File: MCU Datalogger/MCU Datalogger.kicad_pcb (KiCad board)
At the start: 2 copper layers, 50.8 x 30.5 mm, 30 parts, among them J1 Conn_01x04_Pin, J2 Conn_01x09_Pin, J3 Conn_01x04_Pin, J4 Conn_02x03_Odd_Even, U1 24LC1025, U2 DS1337S_, U3 24LC1025, U4 ATMEGA328P-AU, Y1 32.768KHz, Y2 16MHz

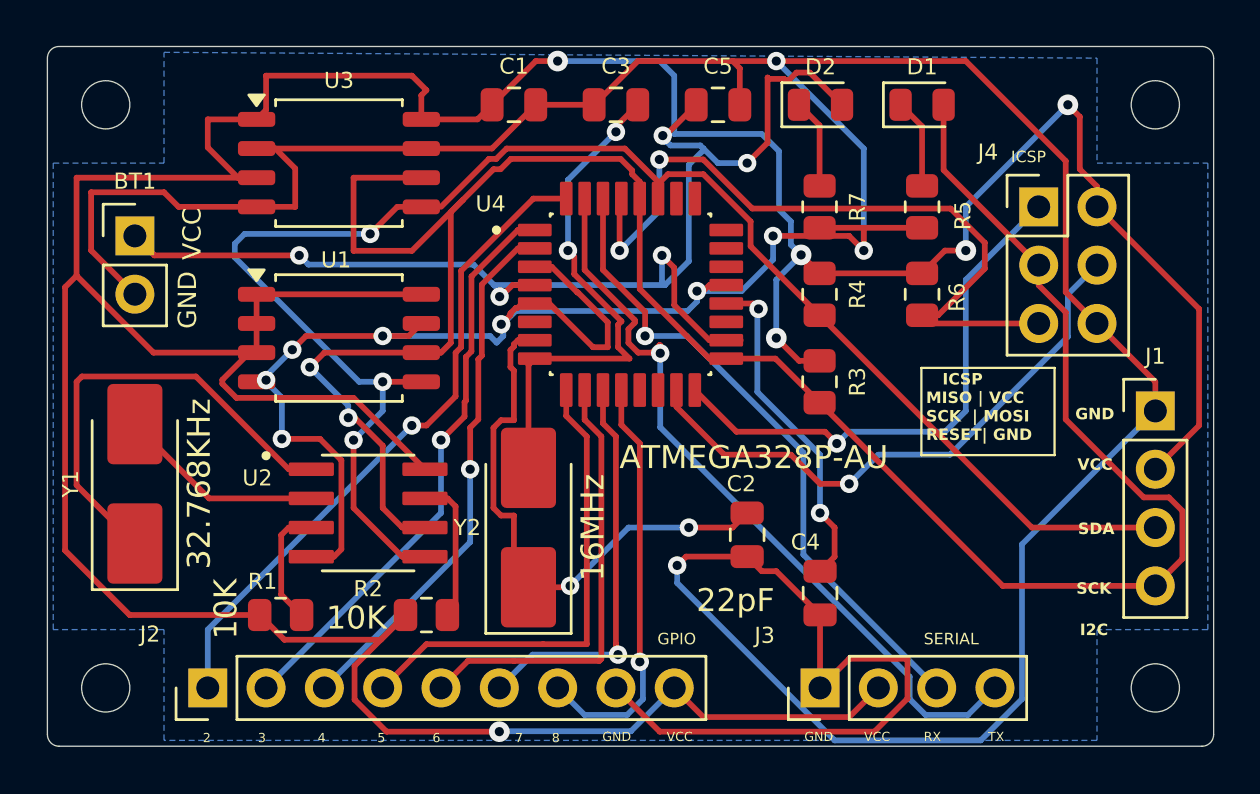
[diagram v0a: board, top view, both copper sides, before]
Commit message: 4layer: Completed 4layer routing of MCUdatalogger
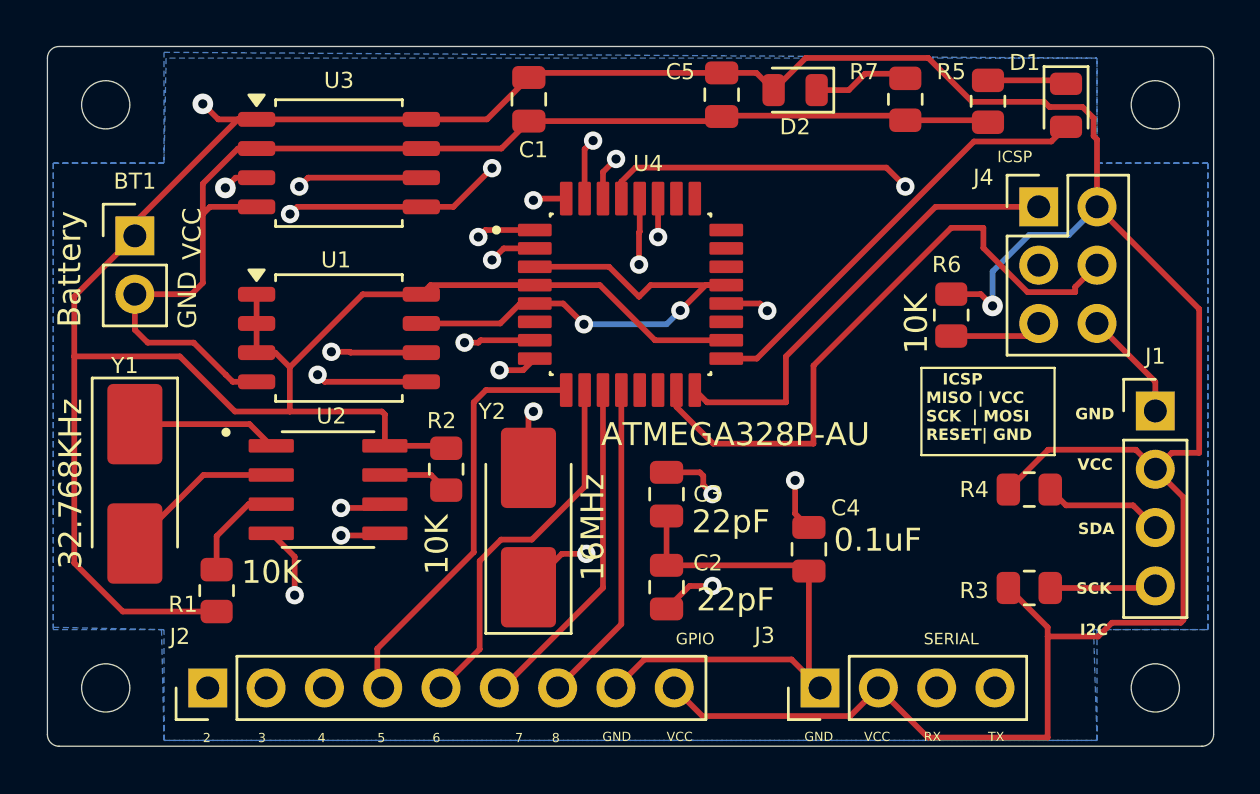
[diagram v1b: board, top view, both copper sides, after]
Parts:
- moved C3 17.1 mm to (140.0, 108.4), turned to 90 degrees
- moved R3 12.8 mm to (155.8, 112.5), turned to 0 degrees
- moved R4 12.5 mm to (155.8, 108.2), turned to 0 degrees
- moved R2 6.41 mm to (130.4, 107.3), turned to -90 degrees
- moved D1 6.27 mm to (157.4, 91.5), turned to -90 degrees
- moved R7 5.99 mm to (150.4, 91.2)
- moved R5 5.42 mm to (154.0, 91.3)
- moved C2 4.19 mm to (140.0, 112.5), turned to -90 degrees
- moved R1 2.99 mm to (120.4, 112.6), turned to 90 degrees
- moved U2 2.02 mm to (125.3, 108.2)
- moved C4 1.97 mm to (146.2, 110.8)
- moved R6 1.56 mm to (152.4, 100.6)
- moved D2 1.28 mm to (145.6, 90.8), turned to 180 degrees
- moved C1 0.69 mm to (134.0, 91.2), turned to -90 degrees
- moved C5 0.47 mm to (142.4, 91.0), turned to -90 degrees
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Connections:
- D1 pad 2: /SCK -> /D9
- U4 pad 17: /SCK -> /D9
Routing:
- net GND: track 208.0 -> 108.8 mm, vias 10 -> 3
- net /Vcc: track 240.0 -> 199.1 mm, vias 11 -> 3
- net /D9: track 0.00 -> 19.0 mm
- net Net-(U2-X1): track 20.1 -> 6.33 mm
- net /RX: track 28.4 -> 37.0 mm
- net /TX: track 34.0 -> 40.7 mm
- net /RESET: track 32.6 -> 26.1 mm, vias 2 -> 1
- net /SCK: track 102.5 -> 96.5 mm, vias 2 -> 4
- net /D8: track 18.3 -> 14.1 mm, vias 1 -> 0
- net Net-(U4-PB7): track 22.5 -> 18.6 mm, vias 2 -> 3
- net /MISO: track 23.6 -> 19.9 mm, vias 1 -> 0
- net Net-(U2-SQW/~INT): track 6.36 -> 2.94 mm
- net /D6: track 19.5 -> 16.4 mm
- net /D7: track 17.6 -> 14.9 mm, vias 1 -> 0
- net /D5: track 21.1 -> 18.5 mm
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- added copper zone on B.Cu, net GND
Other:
- copper layers 2 -> 4
- board text removed: "0.2000 mm / 0.0000 mm"
- board text removed: "0.3000 mm"
- board text removed: "1.6000 mm"
- board text removed: "50.8000 mm x 30.4800 mm"
- board text removed: "BOARD CHARACTERISTICS"
- board text removed: "Board Thickness:"
- board text removed: "Board overall dimensions:"
- board text removed: "Castellated pads:"
- board text removed: "Copper Finish:"
- board text removed: "Copper Layer Count:"
- board text removed: "Edge card connectors:"
- board text removed: "Impedance Control:"
- board text removed: "Min hole diameter:"
- board text removed: "Min track/spacing:"
- board text removed: "No"
- board text removed: "None"
- board text removed: "Plated Board Edge:"

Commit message: 4layer: completed 4 layer routing
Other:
- board text added: "0.2000 mm / 0.0000 mm"
- board text added: "0.3000 mm"
- board text added: "1.6000 mm"
- board text added: "50.8000 mm x 30.4800 mm"
- board text added: "BOARD CHARACTERISTICS"
- board text added: "Board Thickness:"
- board text added: "Board overall dimensions:"
- board text added: "Castellated pads:"
- board text added: "Copper Finish:"
- board text added: "Copper Layer Count:"
- board text added: "Edge card connectors:"
- board text added: "Impedance Control:"
- board text added: "Min hole diameter:"
- board text added: "Min track/spacing:"
- board text added: "No"
- board text added: "None"
- board text added: "Plated Board Edge:"

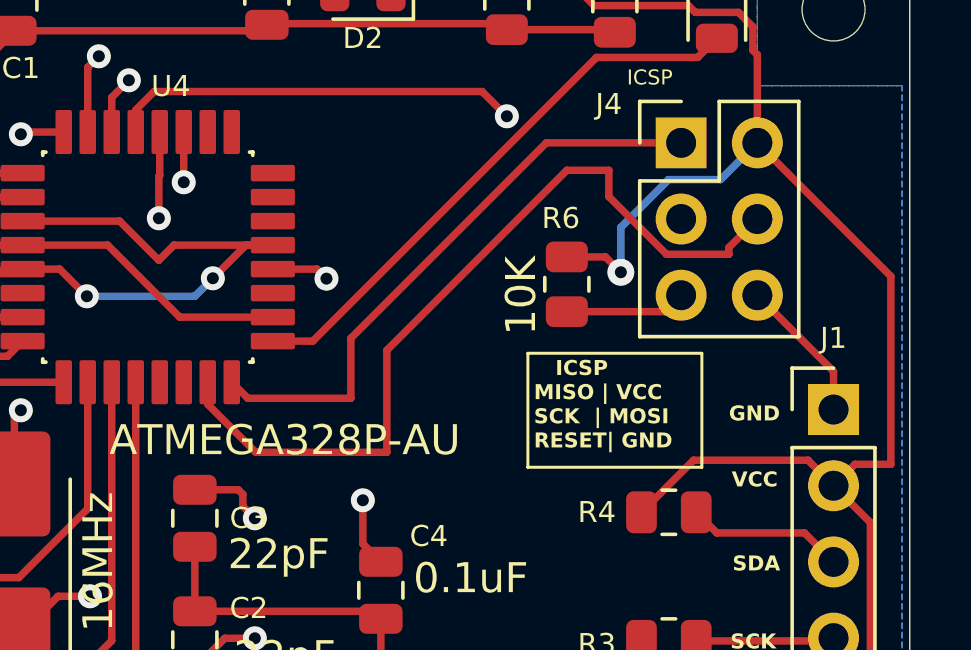
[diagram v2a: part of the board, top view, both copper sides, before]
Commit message: 4layer: recovered and corrected 4layer
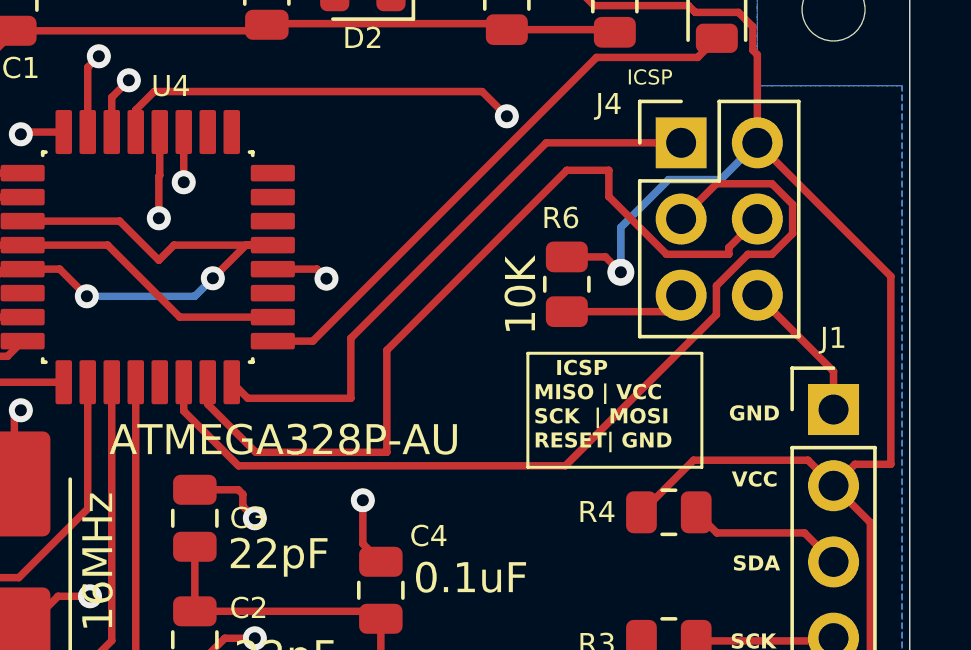
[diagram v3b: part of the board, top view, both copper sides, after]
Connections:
- J1 pad 4: /SCK -> /SCL
- R3 pad 2: /SCK -> /SCL
- U1 pad 6: /SCK -> /SCL
- U2 pad 6: /SCK -> /SCL
- U3 pad 6: /SCK -> /SCL
- U4 pad 14: unconnected-(U4-PB2-Pad14) -> /SCK
- U4 pad 28: /SCK -> /SCL
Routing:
- net /SCL: track 0.00 -> 78.3 mm, vias 0 -> 4
- net /SCK: track 96.5 -> 31.2 mm, vias 4 -> 0
